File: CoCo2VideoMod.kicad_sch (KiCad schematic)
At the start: 36 parts, among them J1 20261043, J2 to PCB, J3 Video, Q1 BC547, Q2 BC557, Q3 BC547, Q4 BC557, Q5 BC547, U1 MC1372P

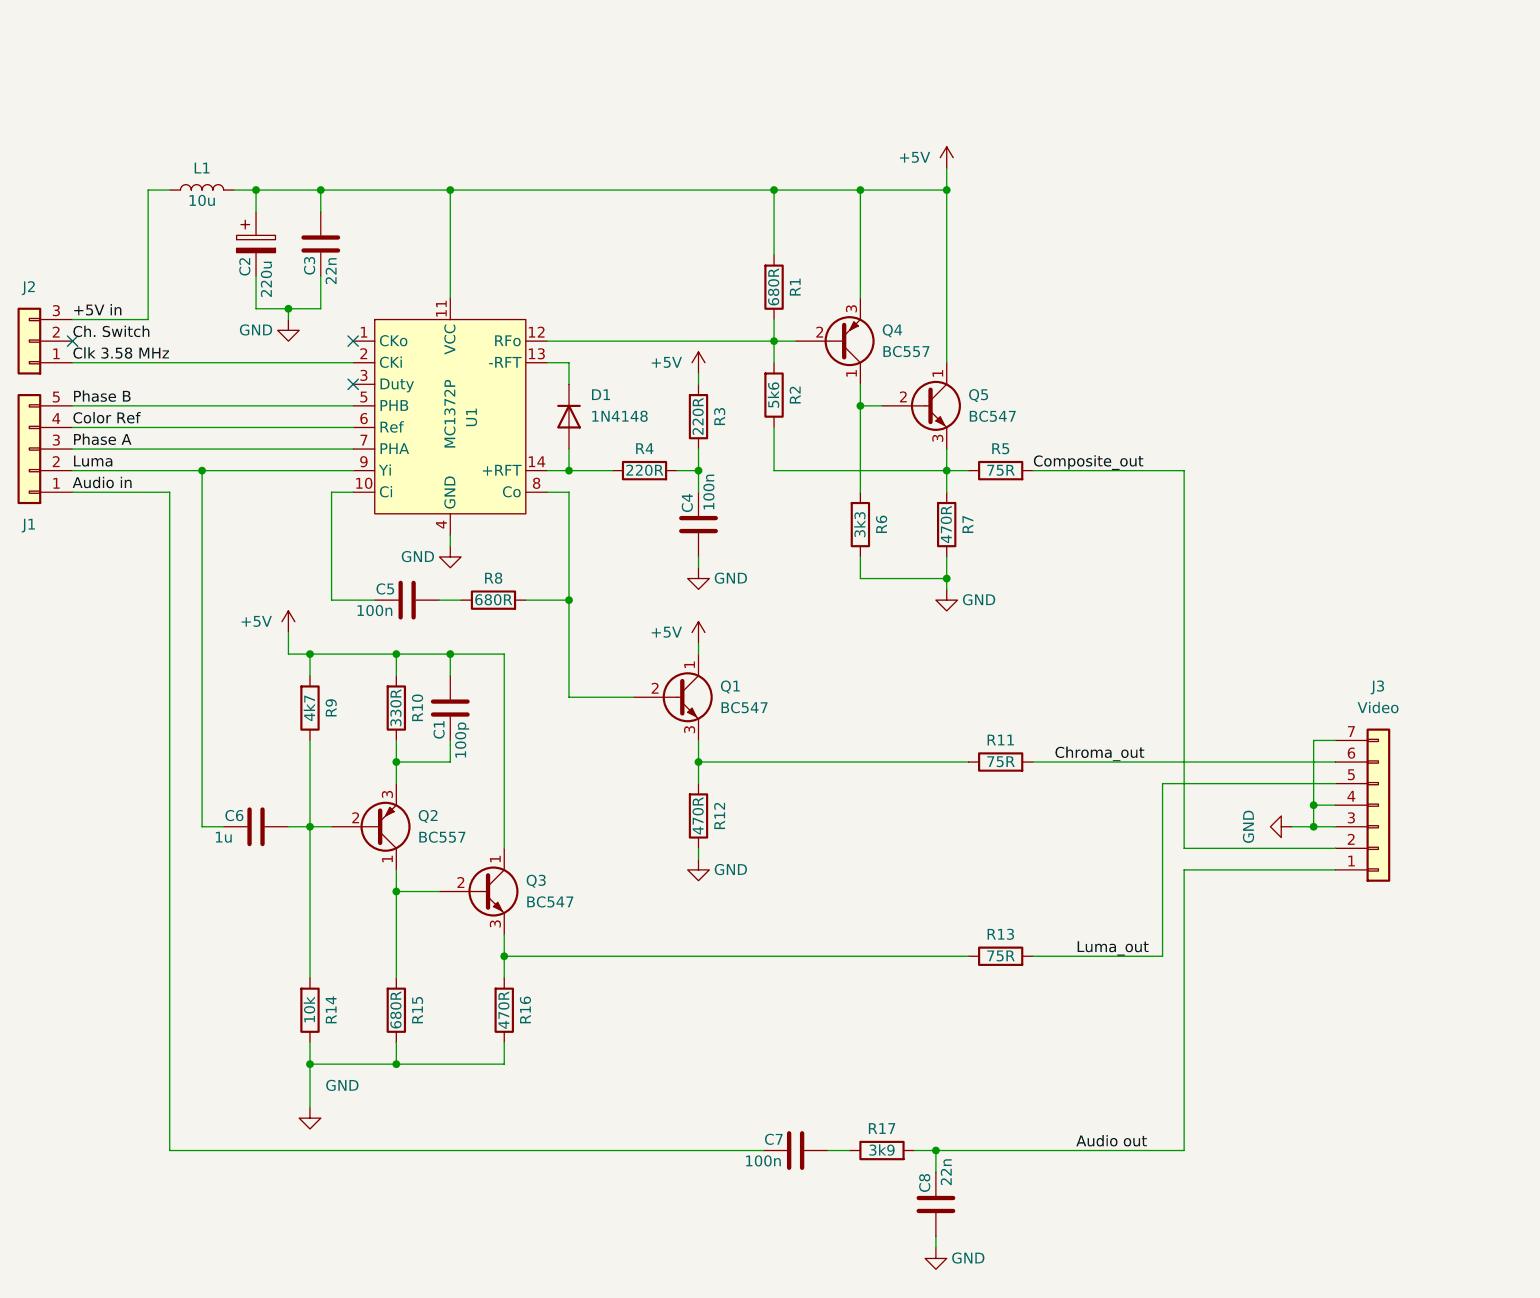
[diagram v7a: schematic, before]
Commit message: rotated connector, added GND pins
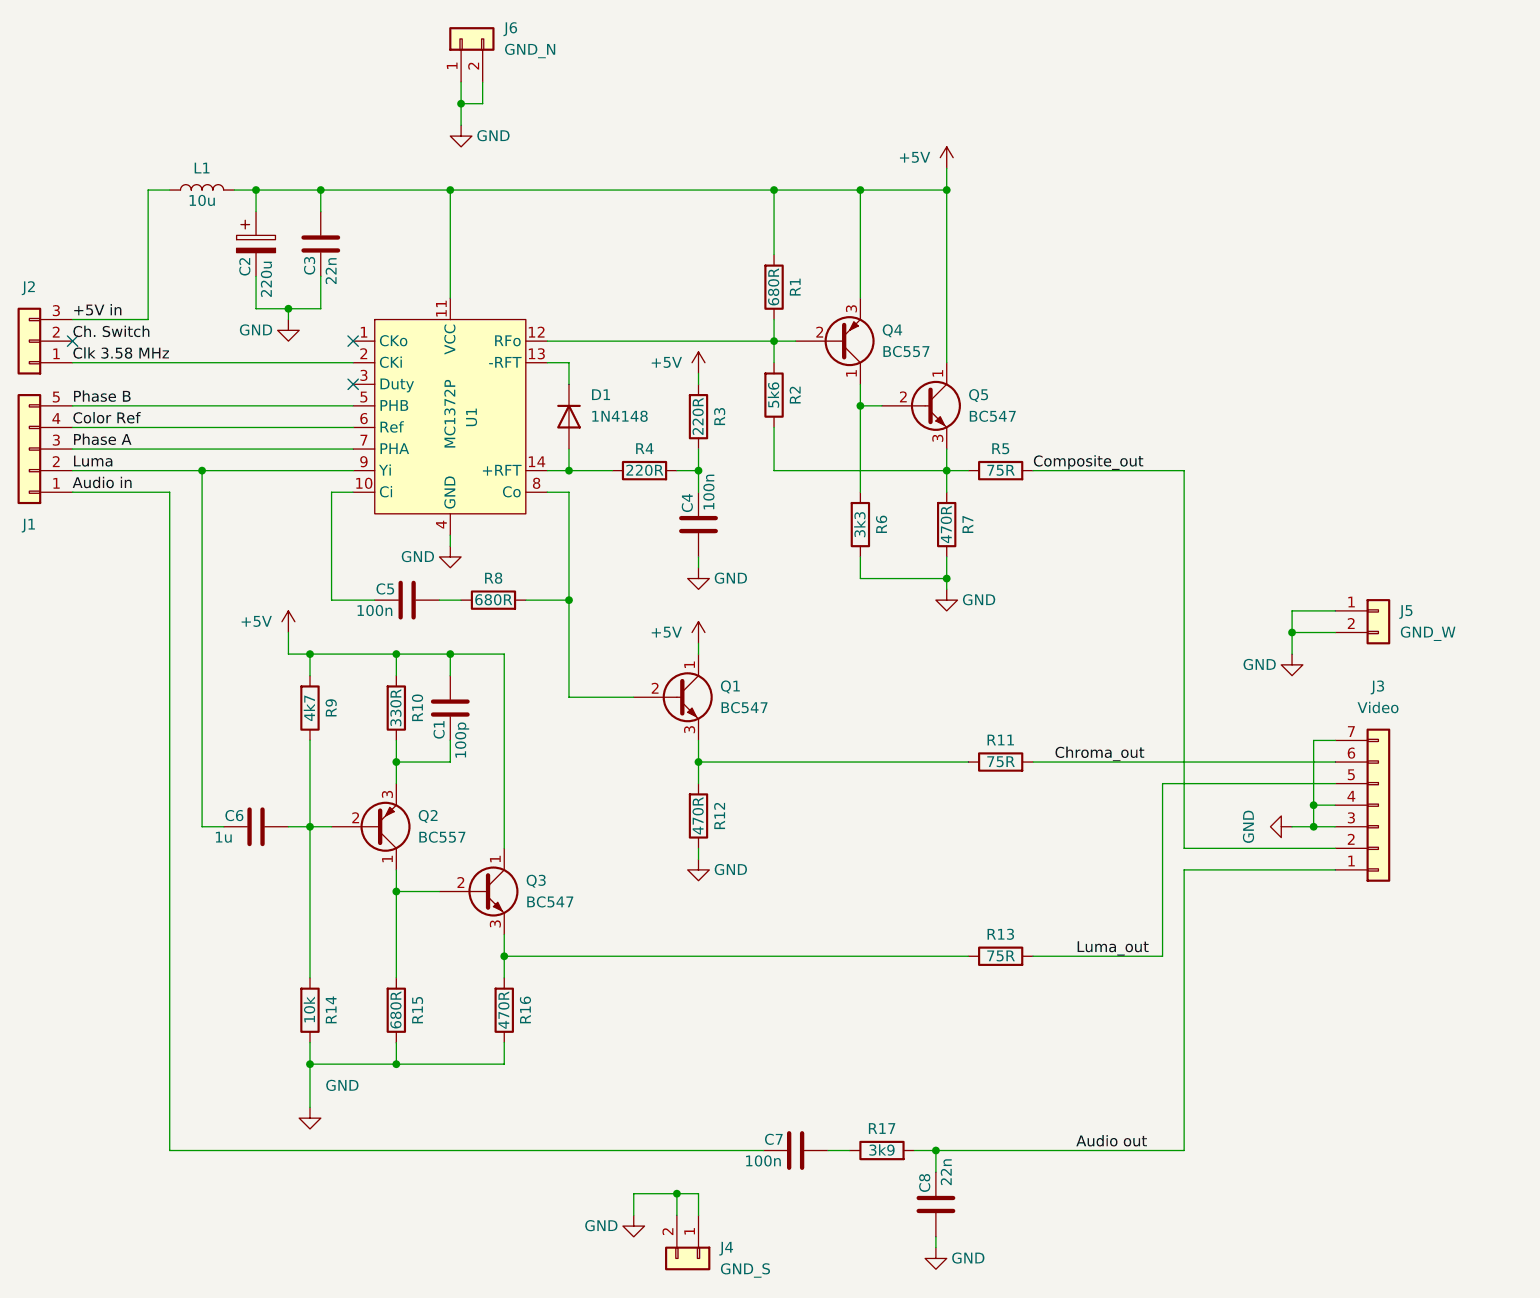
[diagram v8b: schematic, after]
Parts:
- added J4: GND_S, Connector_PinHeader_2.54mm:PinHeader_1x02_P2.54mm_Vertical, symbol Connector_Generic:Conn_01x02
- added J5: GND_W, Connector_PinHeader_2.54mm:PinHeader_1x02_P2.54mm_Vertical, symbol Connector_Generic:Conn_01x02
- added J6: GND_N, Connector_PinHeader_2.54mm:PinHeader_1x02_P2.54mm_Vertical, symbol Connector_Generic:Conn_01x02
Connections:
- net GND: now also J4.1 (Pin_1), J4.2 (Pin_2), J5.1 (Pin_1), J5.2 (Pin_2), J6.1 (Pin_1), J6.2 (Pin_2)
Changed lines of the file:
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@@
     (company "Riven Hexagon Electronics")
   )
+  (junction (at 185.42 90.17) (diameter 0) (color 0 0 0 0)
+  )
   (junction (at 80.01 140.97) (diameter 0) (color 0 0 0 0)
   )
@@
   (junction (at 69.85 92.71) (diameter 0) (color 0 0 0 0)
   )
+  (junction (at 87.63 27.94) (diameter 0) (color 0 0 0 0)
+  )
   (junction (at 115.57 105.41) (diameter 0) (color 0 0 0 0)
   )
@@
   )
   (junction (at 143.51 151.13) (diameter 0) (color 0 0 0 0)
+  )
+  (junction (at 113.03 156.21) (diameter 0) (color 0 0 0 0)
   )
   (junction (at 86.36 38.1) (diameter 0) (color 0 0 0 0)
@@
     (stroke (width 0) (type default))
   )
+  (wire (pts (xy 90.17 27.94) (xy 90.17 25.4))
+    (stroke (width 0) (type default))
+  )
   (wire (pts (xy 115.57 71.12) (xy 113.03 71.12))
     (stroke (width 0) (type default))
@@
     (stroke (width 0) (type default))
   )
+  (wire (pts (xy 185.42 90.17) (xy 185.42 92.71))
+    (stroke (width 0) (type default))
+  )
   (wire (pts (xy 115.57 81.28) (xy 115.57 82.55))
     (stroke (width 0) (type default))
@@
     (stroke (width 0) (type default))
   )
+  (wire (pts (xy 107.95 156.21) (xy 113.03 156.21))
+    (stroke (width 0) (type default))
+  )
   (wire (pts (xy 69.85 113.03) (xy 69.85 102.87))
     (stroke (width 0) (type default))
@@
     (stroke (width 0) (type default))
   )
+  (wire (pts (xy 87.63 27.94) (xy 87.63 30.48))
+    (stroke (width 0) (type default))
+  )
   (wire (pts (xy 185.42 113.03) (xy 187.96 113.03))
     (stroke (width 0) (type default))
@@
     (stroke (width 0) (type default))
   )
+  (wire (pts (xy 107.95 158.75) (xy 107.95 156.21))
+    (stroke (width 0) (type default))
+  )
   (wire (pts (xy 170.18 107.95) (xy 170.18 128.27))
     (stroke (width 0) (type default))
@@
     (stroke (width 0) (type default))
   )
+  (wire (pts (xy 185.42 87.63) (xy 190.5 87.63))
+    (stroke (width 0) (type default))
+  )
   (wire (pts (xy 60.96 38.1) (xy 63.5 38.1))
     (stroke (width 0) (type default))
@@
     (stroke (width 0) (type default))
   )
+  (wire (pts (xy 87.63 27.94) (xy 90.17 27.94))
+    (stroke (width 0) (type default))
+  )
   (wire (pts (xy 100.33 60.96) (xy 100.33 58.42))
     (stroke (width 0) (type default))
@@
     (stroke (width 0) (type default))
   )
+  (wire (pts (xy 185.42 90.17) (xy 185.42 87.63))
+    (stroke (width 0) (type default))
+  )
   (wire (pts (xy 53.34 73.66) (xy 53.34 151.13))
     (stroke (width 0) (type default))
@@
     (stroke (width 0) (type default))
   )
+  (wire (pts (xy 115.57 156.21) (xy 113.03 156.21))
+    (stroke (width 0) (type default))
+  )
   (wire (pts (xy 187.96 102.87) (xy 190.5 102.87))
     (stroke (width 0) (type default))
@@
     (stroke (width 0) (type default))
   )
+  (wire (pts (xy 190.5 90.17) (xy 185.42 90.17))
+    (stroke (width 0) (type default))
+  )
   (wire (pts (xy 67.31 92.71) (xy 67.31 90.17))
     (stroke (width 0) (type default))
@@
     (stroke (width 0) (type default))
   )
+  (wire (pts (xy 87.63 25.4) (xy 87.63 27.94))
+    (stroke (width 0) (type default))
+  )
   (wire (pts (xy 69.85 140.97) (xy 69.85 146.05))
     (stroke (width 0) (type default))
@@
     (stroke (width 0) (type default))
   )
+  (wire (pts (xy 113.03 156.21) (xy 113.03 158.75))
+    (stroke (width 0) (type default))
+  )
   (wire (pts (xy 41.91 58.42) (xy 74.93 58.42))
     (stroke (width 0) (type default))
@@
   )
   (wire (pts (xy 187.96 110.49) (xy 187.96 113.03))
+    (stroke (width 0) (type default))
+  )
+  (wire (pts (xy 115.57 158.75) (xy 115.57 156.21))
     (stroke (width 0) (type default))
   )
@@
         (path "/e26cf8f1-b9bc-4bc2-a425-d53c73655768"
           (reference "#PWR07") (unit 1)
+        )
+      )
+    )
+  )
+  (symbol (lib_id "Connector_Generic:Conn_01x02") (at 115.57 163.83 270) (unit 1)
+    (in_bom yes) (on_board yes) (dnp no) (fields_autoplaced)
+    (property "Reference" "J4" (at 118.11 162.56 90)
+      (effects (font (size 1.27 1.27)) (justify left))
+    )
+    (property "Value" "GND_S" (at 118.11 165.1 90)
+      (effects (font (size 1.27 1.27)) (justify left))
+    )
+    (property "Footprint" "Connector_PinHeader_2.54mm:PinHeader_1x02_P2.54mm_Vertical" (at 115.57 163.83 0)
+      (effects (font (size 1.27 1.27)) hide)
+    )
+    (property "Datasheet" "~" (at 115.57 163.83 0)
+      (effects (font (size 1.27 1.27)) hide)
+    )
+    (pin "1")
+    (pin "2")
+    (instances
+      (project "CoCo2VideoMod"
+        (path "/e26cf8f1-b9bc-4bc2-a425-d53c73655768"
+          (reference "J4") (unit 1)
         )
       )
@@
         (path "/e26cf8f1-b9bc-4bc2-a425-d53c73655768"
           (reference "R16") (unit 1)
+        )
+      )
+    )
+  )
+  (symbol (lib_id "Connector_Generic:Conn_01x02") (at 87.63 20.32 90) (unit 1)
+    (in_bom yes) (on_board yes) (dnp no) (fields_autoplaced)
+    (property "Reference" "J6" (at 92.71 19.05 90)
+      (effects (font (size 1.27 1.27)) (justify right))
+    )
+    (property "Value" "GND_N" (at 92.71 21.59 90)
+      (effects (font (size 1.27 1.27)) (justify right))
+    )
+    (property "Footprint" "Connector_PinHeader_2.54mm:PinHeader_1x02_P2.54mm_Vertical" (at 87.63 20.32 0)
+      (effects (font (size 1.27 1.27)) hide)
+    )
+    (property "Datasheet" "~" (at 87.63 20.32 0)
+      (effects (font (size 1.27 1.27)) hide)
+    )
+    (pin "1")
+    (pin "2")
+    (instances
+      (project "CoCo2VideoMod"
+        (path "/e26cf8f1-b9bc-4bc2-a425-d53c73655768"
+          (reference "J6") (unit 1)
         )
       )
@@
     )
   )
+  (symbol (lib_id "power:GND") (at 87.63 30.48 0) (unit 1)
+    (in_bom yes) (on_board yes) (dnp no)
+    (property "Reference" "#PWR015" (at 87.63 36.83 0)
+      (effects (font (size 1.27 1.27)) hide)
+    )
+    (property "Value" "GND" (at 91.44 31.75 0)
+      (effects (font (size 1.27 1.27)))
+    )
+    (property "Footprint" "" (at 87.63 30.48 0)
+      (effects (font (size 1.27 1.27)) hide)
+    )
+    (property "Datasheet" "" (at 87.63 30.48 0)
+      (effects (font (size 1.27 1.27)) hide)
+    )
+    (pin "1")
+    (instances
+      (project "CoCo2VideoMod"
+        (path "/e26cf8f1-b9bc-4bc2-a425-d53c73655768"
+          (reference "#PWR015") (unit 1)
+        )
+      )
+    )
+  )
   (symbol (lib_id "Device:C") (at 115.57 77.47 0) (mirror x) (unit 1)
     (in_bom yes) (on_board yes) (dnp no)
@@
     )
   )
+  (symbol (lib_id "power:GND") (at 107.95 158.75 0) (unit 1)
+    (in_bom yes) (on_board yes) (dnp no)
+    (property "Reference" "#PWR013" (at 107.95 165.1 0)
+      (effects (font (size 1.27 1.27)) hide)
+    )
+    (property "Value" "GND" (at 104.14 160.02 0)
+      (effects (font (size 1.27 1.27)))
+    )
+    (property "Footprint" "" (at 107.95 158.75 0)
+      (effects (font (size 1.27 1.27)) hide)
+    )
+    (property "Datasheet" "" (at 107.95 158.75 0)
+      (effects (font (size 1.27 1.27)) hide)
+    )
+    (pin "1")
+    (instances
+      (project "CoCo2VideoMod"
+        (path "/e26cf8f1-b9bc-4bc2-a425-d53c73655768"
+          (reference "#PWR013") (unit 1)
+        )
+      )
+    )
+  )
   (symbol (lib_id "Device:R") (at 151.13 128.27 90) (unit 1)
     (in_bom yes) (on_board yes) (dnp no)
@@
         (path "/e26cf8f1-b9bc-4bc2-a425-d53c73655768"
           (reference "C7") (unit 1)
+        )
+      )
+    )
+  )
+  (symbol (lib_id "Connector_Generic:Conn_01x02") (at 195.58 87.63 0) (unit 1)
+    (in_bom yes) (on_board yes) (dnp no) (fields_autoplaced)
+    (property "Reference" "J5" (at 198.12 87.63 0)
+      (effects (font (size 1.27 1.27)) (justify left))
+    )
+    (property "Value" "GND_W" (at 198.12 90.17 0)
+      (effects (font (size 1.27 1.27)) (justify left))
+    )
+    (property "Footprint" "Connector_PinHeader_2.54mm:PinHeader_1x02_P2.54mm_Vertical" (at 195.58 87.63 0)
+      (effects (font (size 1.27 1.27)) hide)
+    )
+    (property "Datasheet" "~" (at 195.58 87.63 0)
+      (effects (font (size 1.27 1.27)) hide)
+    )
+    (pin "1")
+    (pin "2")
+    (instances
+      (project "CoCo2VideoMod"
+        (path "/e26cf8f1-b9bc-4bc2-a425-d53c73655768"
+          (reference "J5") (unit 1)
         )
       )
@@
         )
       )
+    )
+  )
+  (symbol (lib_id "power:GND") (at 185.42 92.71 0) (unit 1)
+    (in_bom yes) (on_board yes) (dnp no)
+    (property "Reference" "#PWR014" (at 185.42 99.06 0)
+      (effects (font (size 1.27 1.27)) hide)
+    )
+    (property "Value" "GND" (at 181.61 93.98 0)
+      (effects (font (size 1.27 1.27)))
+    )
+    (property "Footprint" "" (at 185.42 92.71 0)
+      (effects (font (size 1.27 1.27)) hide)
+    )
+    (property "Datasheet" "" (at 185.42 92.71 0)
+      (effects (font (size 1.27 1.27)) hide)
+    )
+    (pin "1")
+    (instances
+      (project "CoCo2VideoMod"
+        (path "/e26cf8f1-b9bc-4bc2-a425-d53c73655768"
+          (reference "#PWR014") (unit 1)
+        )
+      )
